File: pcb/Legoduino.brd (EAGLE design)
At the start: 80 x 80 mm, 91 parts, among them CON11 ISP-AVR, CON2 PIN(1+16)X3_DS, IC1 NCP3170ADR2G, IC2 RN-42, IC3 MIC5205-5.0YM5, IC4 ATMEGA2560-16AU, IC5 UG-2864HSWEG01_SPI, IC6 MIC5205-3.6YM5, IC7 MIC5205-3.3YM5, IC8 BD6221F-E2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

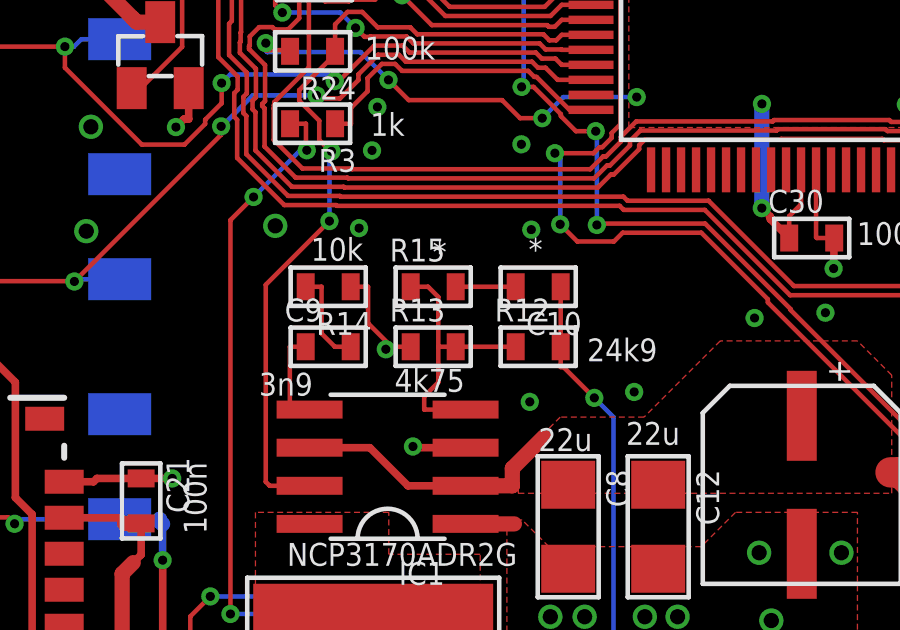
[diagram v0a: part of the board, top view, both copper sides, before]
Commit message: Updated feedback compensation circuit for NCP3170
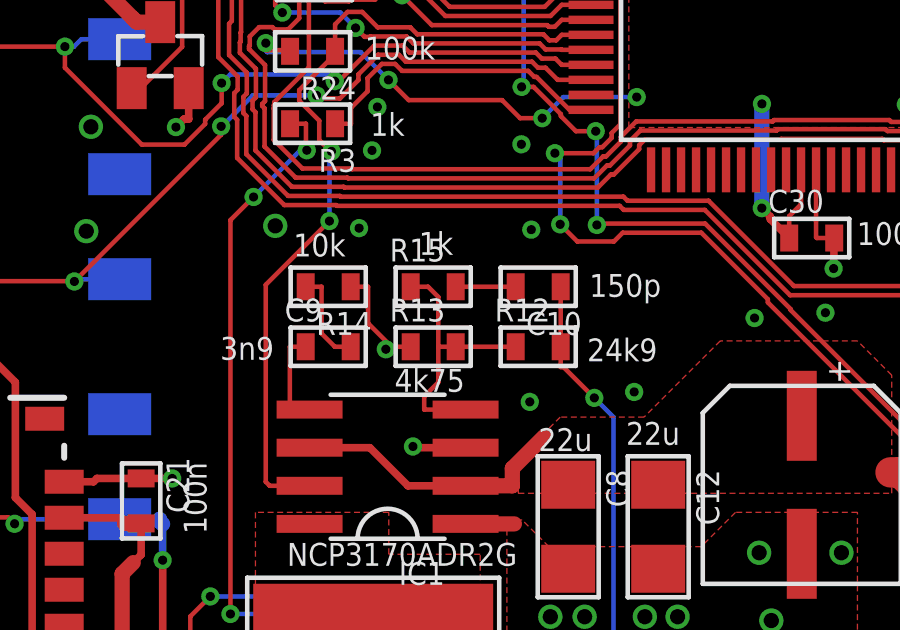
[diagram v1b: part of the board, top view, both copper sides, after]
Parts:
- C10: value * -> 150p
- R15: value * -> 1k
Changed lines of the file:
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@@
 <layer number="23" name="tOrigins" color="15" fill="1" visible="yes" active="yes"/>
 <layer number="24" name="bOrigins" color="15" fill="1" visible="yes" active="yes"/>
-<layer number="25" name="tNames" color="7" fill="1" visible="yes" active="yes"/>
-<layer number="26" name="bNames" color="7" fill="1" visible="yes" active="yes"/>
-<layer number="27" name="tValues" color="7" fill="1" visible="no" active="yes"/>
-<layer number="28" name="bValues" color="7" fill="1" visible="no" active="yes"/>
+<layer number="25" name="tNames" color="7" fill="1" visible="no" active="yes"/>
+<layer number="26" name="bNames" color="7" fill="1" visible="no" active="yes"/>
+<layer number="27" name="tValues" color="7" fill="1" visible="yes" active="yes"/>
+<layer number="28" name="bValues" color="7" fill="1" visible="yes" active="yes"/>
 <layer number="29" name="tStop" color="7" fill="3" visible="no" active="yes"/>
 <layer number="30" name="bStop" color="7" fill="6" visible="no" active="yes"/>
@@
 <layer number="97" name="Info" color="7" fill="1" visible="no" active="no"/>
 <layer number="98" name="Guide" color="6" fill="1" visible="no" active="no"/>
-<layer number="100" name="tSilk2" color="7" fill="1" visible="no" active="yes"/>
-<layer number="101" name="bSilk2" color="7" fill="1" visible="no" active="yes"/>
+<layer number="100" name="tSilk2" color="7" fill="1" visible="yes" active="yes"/>
+<layer number="101" name="bSilk2" color="7" fill="1" visible="yes" active="yes"/>
 <layer number="108" name="fp8" color="7" fill="1" visible="no" active="no"/>
 <layer number="109" name="fp9" color="7" fill="1" visible="no" active="no"/>
@@
 <element name="R14" library="PN_default" package="0603" value="10k" x="31" y="38" smashed="yes" rot="R180">
 <attribute name="NAME" x="32.451" y="37.157" size="0.762" layer="25" font="vector" ratio="20" rot="R180"/>
-<attribute name="VALUE" x="32.163" y="39.629" size="0.762" layer="100" font="vector" ratio="20" rot="R180"/>
+<attribute name="VALUE" x="29.8384" y="39.0094" size="0.762" layer="100" font="vector" ratio="20"/>
 </element>
 <element name="C2" library="PN_default" package="1206" value="22u" x="42" y="24" smashed="yes" rot="R90">
@@
 <element name="C9" library="PN_default" package="0603" value="3n9" x="31" y="36" smashed="yes">
 <attribute name="NAME" x="29.549" y="36.843" size="0.762" layer="25" font="vector" ratio="20"/>
-<attribute name="VALUE" x="28.694" y="34.371" size="0.762" layer="100" font="vector" ratio="20"/>
-</element>
-<element name="R15" library="PN_default" package="0603" value="*" x="34.5" y="38" smashed="yes">
+<attribute name="VALUE" x="27.3986" y="35.5648" size="0.762" layer="100" font="vector" ratio="20"/>
+</element>
+<element name="R15" library="PN_default" package="0603" value="1k" x="34.5" y="38" smashed="yes">
 <attribute name="NAME" x="33.049" y="38.843" size="0.762" layer="25" font="vector" ratio="20"/>
-<attribute name="VALUE" x="34.48" y="38.784" size="0.762" layer="100" font="vector" ratio="20"/>
-</element>
-<element name="C10" library="PN_default" package="0603" value="*" x="38" y="38" smashed="yes" rot="R180">
+<attribute name="VALUE" x="34.0228" y="39.0634" size="0.762" layer="100" font="vector" ratio="20"/>
+</element>
+<element name="C10" library="PN_default" package="0603" value="150p" x="38" y="38" smashed="yes" rot="R180">
 <attribute name="NAME" x="39.451" y="37.157" size="0.762" layer="25" font="vector" ratio="20" rot="R180"/>
-<attribute name="VALUE" x="38.147" y="39.629" size="0.762" layer="100" font="vector" ratio="20" rot="R180"/>
+<attribute name="VALUE" x="39.704" y="37.6632" size="0.762" layer="100" font="vector" ratio="20"/>
 </element>
 <element name="C11" library="PN_default" package="1206" value="22u" x="39" y="24" smashed="yes" rot="R90">

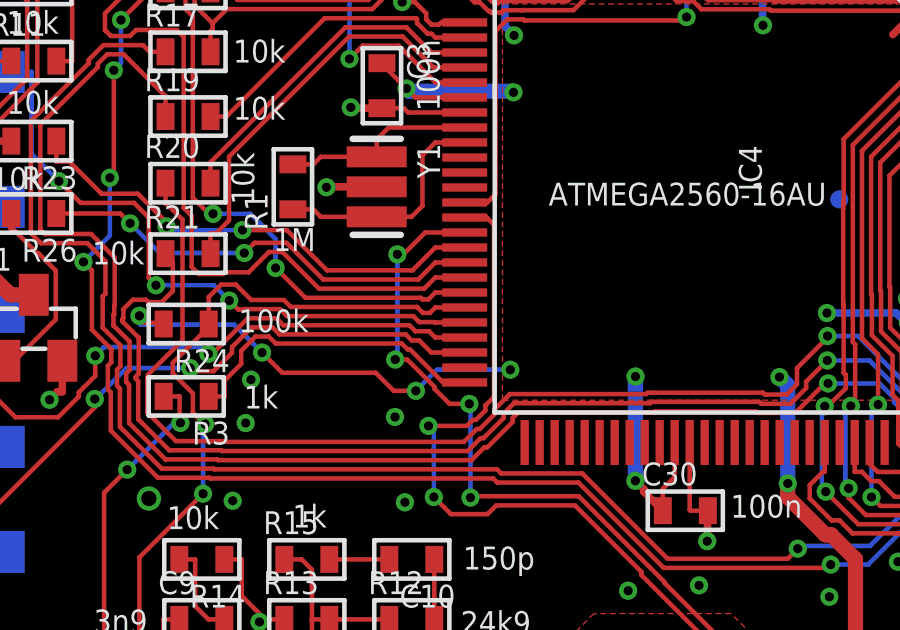
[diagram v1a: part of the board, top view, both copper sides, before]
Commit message: Updated net names according to Arduino Mega pin numbers
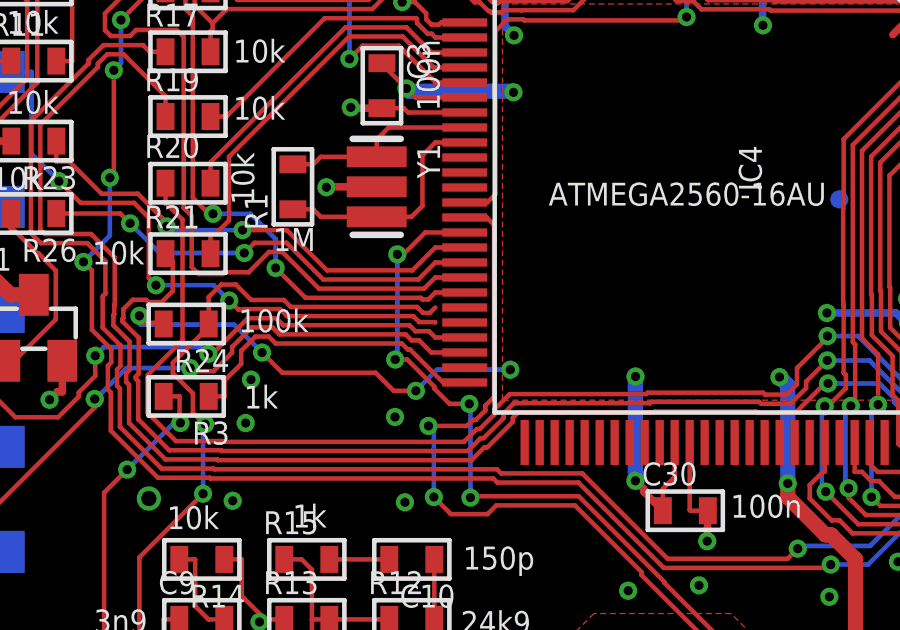
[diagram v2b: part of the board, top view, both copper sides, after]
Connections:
- net BT_RST renamed 43
- net BUZZ renamed 42
- net LED renamed 38
- net MISO renamed 50
- net MOSI renamed 51
- net PA4 renamed 26
- net PA5 renamed 27
- net PB4 renamed 10
- net PB5 renamed 11
- net PB6 renamed 12
- net PB7 renamed 13
- net PD5 renamed 22
- net PD6 renamed 23
- net PD7 renamed 24
- net PE0 renamed 0
- net PE1 renamed 1
- net PE3 renamed 5
- net PE4 renamed 2
- net PE5 renamed 3
- net PG5 renamed 4
- net PH3 renamed 6
- net PH4 renamed 7
- net PH5 renamed 8
- net PH6 renamed 9
- net PL3 renamed 45
- net PL4 renamed 46
- net PL5 renamed 44
- net PL7 renamed 29
- net SCK renamed 52
- net SCL renamed 21
- net SDA renamed 20
- new net 18: IC4.46
- new net 19: IC4.45
- net +5VP_PG: no longer IC4.45
- net SW3: no longer IC4.46
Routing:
- net SW3: track 40.1 -> 39.1 mm
- net +5VP_PG: track 27.9 -> 26.9 mm
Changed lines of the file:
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@@
 <wire x1="58.4197" y1="46.48" x2="56.642" y2="46.48" width="0.1524" layer="16"/>
 </signal>
-<signal name="SDA">
+<signal name="20">
 <contactref element="JP6" pad="2"/>
 <contactref element="R6" pad="1"/>
@@
 <wire x1="26.7466" y1="61.71" x2="26.67" y2="61.71" width="0.1524" layer="1"/>
 </signal>
-<signal name="SCL">
+<signal name="21">
 <contactref element="JP6" pad="1"/>
 <contactref element="R5" pad="1"/>
@@
 <wire x1="61.087" y1="41.603" x2="63.96" y2="38.73" width="0.1524" layer="1"/>
 </signal>
-<signal name="MISO">
+<signal name="50">
 <contactref element="CON11" pad="1"/>
 <contactref element="IC4" pad="22"/>
@@
 <wire x1="11.3189" y1="66.675" x2="10.541" y2="66.675" width="0.1524" layer="1"/>
 </signal>
-<signal name="MOSI">
+<signal name="51">
 <contactref element="CON11" pad="4"/>
 <contactref element="IC4" pad="21"/>
@@
 <wire x1="14.8173" y1="65.1135" x2="14.5051" y2="64.8013" width="0.1524" layer="1"/>
 </signal>
-<signal name="SCK">
+<signal name="52">
 <contactref element="CON11" pad="3"/>
 <contactref element="IC4" pad="20"/>
@@
 <wire x1="13.8424" y1="64.2415" x2="13.2827" y2="64.8012" width="0.1524" layer="1"/>
 </signal>
-<signal name="PB5">
+<signal name="11">
 <contactref element="JP6" pad="7"/>
 <contactref element="IC4" pad="24"/>
@@
 <wire x1="42.262" y1="60.989" x2="39.116" y2="64.135" width="0.1524" layer="1"/>
 </signal>
-<signal name="PB4">
+<signal name="10">
 <contactref element="JP6" pad="8"/>
 <contactref element="IC4" pad="23"/>
@@
 <wire x1="42.762" y1="63.029" x2="41.656" y2="64.135" width="0.1524" layer="1"/>
 </signal>
-<signal name="PE5">
+<signal name="3">
 <contactref element="PWML" pad="4"/>
 <contactref element="IC4" pad="7"/>
@@
 <wire x1="56.7956" y1="65.7594" x2="58.42" y2="64.135" width="0.1524" layer="1"/>
 </signal>
-<signal name="PE4">
+<signal name="2">
 <contactref element="PWML" pad="3"/>
 <contactref element="IC4" pad="6"/>
@@
 <wire x1="54.5671" y1="65.4479" x2="55.88" y2="64.135" width="0.1524" layer="1"/>
 </signal>
-<signal name="PE3">
+<signal name="5">
 <contactref element="PWML" pad="6"/>
 <contactref element="IC4" pad="5"/>
@@
 <wire x1="62.6026" y1="64.135" x2="63.5" y2="64.135" width="0.1524" layer="1"/>
 </signal>
-<signal name="PE1">
+<signal name="1">
 <contactref element="PWML" pad="2"/>
 <contactref element="R11" pad="2"/>
@@
 <wire x1="28.8912" y1="58.2613" x2="30.6374" y2="60.0075" width="0.1524" layer="16"/>
 </signal>
-<signal name="PE0">
+<signal name="0">
 <contactref element="PWML" pad="1"/>
 <contactref element="R10" pad="2"/>
@@
 <wire x1="27.7424" y1="40.2229" x2="28.5122" y2="40.9927" width="0.1524" layer="1"/>
 </signal>
-<signal name="PB6">
+<signal name="12">
 <contactref element="JP6" pad="6"/>
 <contactref element="IC4" pad="25"/>
@@
 <wire x1="41.762" y1="58.949" x2="36.576" y2="64.135" width="0.1524" layer="1"/>
 </signal>
-<signal name="PH3">
+<signal name="6">
 <contactref element="PWML" pad="7"/>
 <contactref element="IC4" pad="15"/>
@@
 <wire x1="46.762" y1="57.1722" x2="46.762" y2="57.897" width="0.1524" layer="1"/>
 </signal>
-<signal name="PH4">
+<signal name="7">
 <contactref element="PWML" pad="8"/>
 <contactref element="IC4" pad="16"/>
@@
 <wire x1="46.262" y1="57.1772" x2="46.262" y2="57.897" width="0.1524" layer="1"/>
 </signal>
-<signal name="PH5">
+<signal name="8">
 <contactref element="JP6" pad="10"/>
 <contactref element="IC4" pad="17"/>
@@
 <wire x1="45.762" y1="63.161" x2="45.762" y2="57.897" width="0.1524" layer="1"/>
 </signal>
-<signal name="PH6">
+<signal name="9">
 <contactref element="JP6" pad="9"/>
 <contactref element="IC4" pad="18"/>
@@
 <wire x1="45.262" y1="63.069" x2="44.196" y2="64.135" width="0.1524" layer="1"/>
 </signal>
-<signal name="PG5">
+<signal name="4">
 <contactref element="PWML" pad="5"/>
 <contactref element="IC4" pad="1"/>
@@
 <wire x1="59.0261" y1="62.2011" x2="60.96" y2="64.135" width="0.1524" layer="1"/>
 </signal>
-<signal name="PD7">
+<signal name="24">
 <contactref element="IC4" pad="76"/>
 <contactref element="CON2" pad="15"/>
@@
 <wire x1="57.23" y1="43.897" x2="55.762" y2="43.897" width="0.1524" layer="1"/>
 </signal>
-<signal name="PL3">
+<signal name="45">
 <contactref element="IC4" pad="39"/>
 <contactref element="CON2" pad="6"/>
@@
 <wire x1="40.4961" y1="49.397" x2="39.762" y2="49.397" width="0.1524" layer="1"/>
 </signal>
-<signal name="PL4">
+<signal name="46">
 <contactref element="IC4" pad="38"/>
 <contactref element="IC9" pad="4"/>
@@
 <wire x1="61.9712" y1="69.8502" x2="62.605" y2="70.484" width="0.1524" layer="1"/>
 </signal>
-<signal name="PL5">
+<signal name="44">
 <contactref element="IC4" pad="40"/>
 <contactref element="IC8" pad="4"/>
@@
 <wire x1="37.8465" y1="44.6623" x2="37.4468" y2="44.6623" width="0.1524" layer="1"/>
 </signal>
-<signal name="PB7">
+<signal name="13">
 <contactref element="JP6" pad="5"/>
 <contactref element="IC4" pad="26"/>
@@
 </polygon>
 </signal>
-<signal name="PD6">
+<signal name="23">
 <contactref element="IC4" pad="77"/>
 <contactref element="CON2" pad="18"/>
@@
 <wire x1="57.1613" y1="44.397" x2="55.762" y2="44.397" width="0.1524" layer="1"/>
 </signal>
-<signal name="PD5">
+<signal name="22">
 <contactref element="IC4" pad="78"/>
 <contactref element="CON2" pad="21"/>
@@
 <wire x1="56.5241" y1="43.0259" x2="56.5192" y2="43.0308" width="0.1524" layer="16"/>
 </signal>
-<signal name="LED">
+<signal name="38">
 <contactref element="R3" pad="1"/>
 <contactref element="IC4" pad="50"/>
@@
 <wire x1="24.0705" y1="51.943" x2="24.65" y2="51.943" width="0.254" layer="1"/>
 </signal>
-<signal name="BT_RST">
+<signal name="43">
 <contactref element="R23" pad="1"/>
 <contactref element="IC4" pad="41"/>
@@
 <wire x1="24.65" y1="49.3685" x2="24.65" y2="49.071" width="0.254" layer="1"/>
 </signal>
-<signal name="BUZZ">
+<signal name="42">
 <contactref element="R26" pad="1"/>
 <contactref element="IC4" pad="42"/>
@@
 <signal name="+5VP_PG">
 <contactref element="IC1" pad="7"/>
-<contactref element="IC4" pad="45"/>
 <contactref element="R24" pad="1"/>
-<wire x1="39.762" y1="46.397" x2="38.7833" y2="46.397" width="0.1524" layer="1"/>
 <wire x1="38.7833" y1="46.397" x2="38.6013" y2="46.215" width="0.1524" layer="1"/>
 <wire x1="38.6013" y1="46.215" x2="38.3739" y2="46.215" width="0.1524" layer="1"/>
@@
 <wire x1="50.5518" y1="70.5072" x2="47.3306" y2="67.286" width="0.1524" layer="1"/>
 </signal>
-<signal name="PL7">
+<signal name="29">
 <contactref element="IC4" pad="71"/>
 <contactref element="IC8" pad="5"/>
@@
 <wire x1="51.762" y1="41.897" x2="51.762" y2="40.9183" width="0.1524" layer="1"/>
 </signal>
-<signal name="PA4">
+<signal name="26">
 <contactref element="IC4" pad="74"/>
 <contactref element="CON2" pad="12"/>
@@
 <via x="60.1831" y="29.7866" extent="1-16" drill="0.3048" diameter="0.6096"/>
 </signal>
-<signal name="PA5">
+<signal name="27">
 <contactref element="IC4" pad="73"/>
 <contactref element="CON2" pad="9"/>
@@
 <contactref element="SW3" pad="1A"/>
 <contactref element="SW3" pad="1"/>
-<contactref element="IC4" pad="46"/>
-<wire x1="39.762" y1="45.897" x2="38.7833" y2="45.897" width="0.1524" layer="1"/>
 <wire x1="38.7833" y1="45.897" x2="38.7702" y2="45.9101" width="0.1524" layer="1"/>
 <wire x1="38.7702" y1="45.9101" x2="38.2475" y2="45.9101" width="0.1524" layer="1"/>
@@
 <wire x1="66.416" y1="23.49" x2="66.5" y2="23.49" width="0.762" layer="1"/>
 </signal>
+<signal name="19">
+<contactref element="IC4" pad="45"/>
+</signal>
+<signal name="18">
+<contactref element="IC4" pad="46"/>
+</signal>
 </signals>

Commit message: Updated net names according to Arduino Mega pin numbers
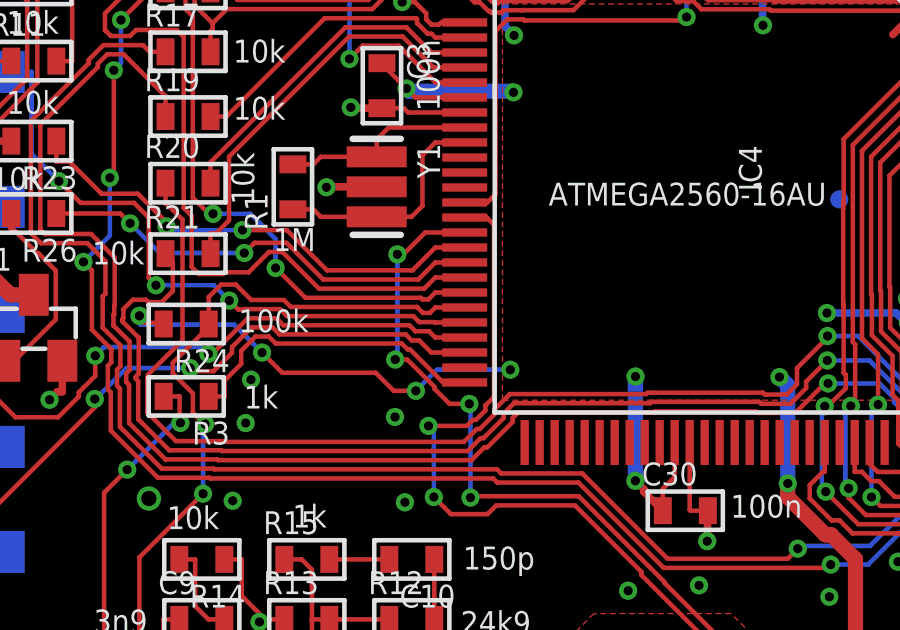
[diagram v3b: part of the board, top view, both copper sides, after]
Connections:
- net !OLED_CS renamed 72
- net !OLED_RST renamed 73
- net OLED_D/!C renamed 70
- net PL6 renamed 71
- net SW1 renamed 75
- net SW2 renamed 74
- removed net +5VP_PG: IC1.7, R24.1
- removed net SW3: SW3.1, SW3.1A
- net 18: now also SW3.1, SW3.1A
- net 19: now also IC1.7, R24.1
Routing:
- net 18: track 0.00 -> 40.1 mm, vias 0 -> 5
- net SW3: track 39.1 -> 0.00 mm, vias 5 -> 0
- net 19: track 0.00 -> 27.9 mm, vias 0 -> 2
- net +5VP_PG: track 26.9 -> 0.00 mm, vias 2 -> 0
